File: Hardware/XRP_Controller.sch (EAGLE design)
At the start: 75 parts, among them J1 POWER_JACKPOWER_JACK_SLOT, J12 Vertical Qwiic Connector, J13 Vertical Qwiic Connector, J14 Vertical Qwiic Connector, J3 JST_6_PIN_VERTICAL, J4 JST_6_PIN_VERTICAL, J5 JST_6_PIN_VERTICAL, J6 JST_6_PIN_VERTICAL, J9 Vertical Qwiic Connector, Q3 20V/4.2A/52mΩ/1.4W, Q4 20V/4.2A/52mΩ/1.4W, Q5 20V/4.2A/52mΩ/1.4W, Q6 20V/4.2A/52mΩ/1.4W, U1 RPI_PICO_W, U2 AP63357, U4 LSM6DS0, U5 DRV8835, U6 DRV8835

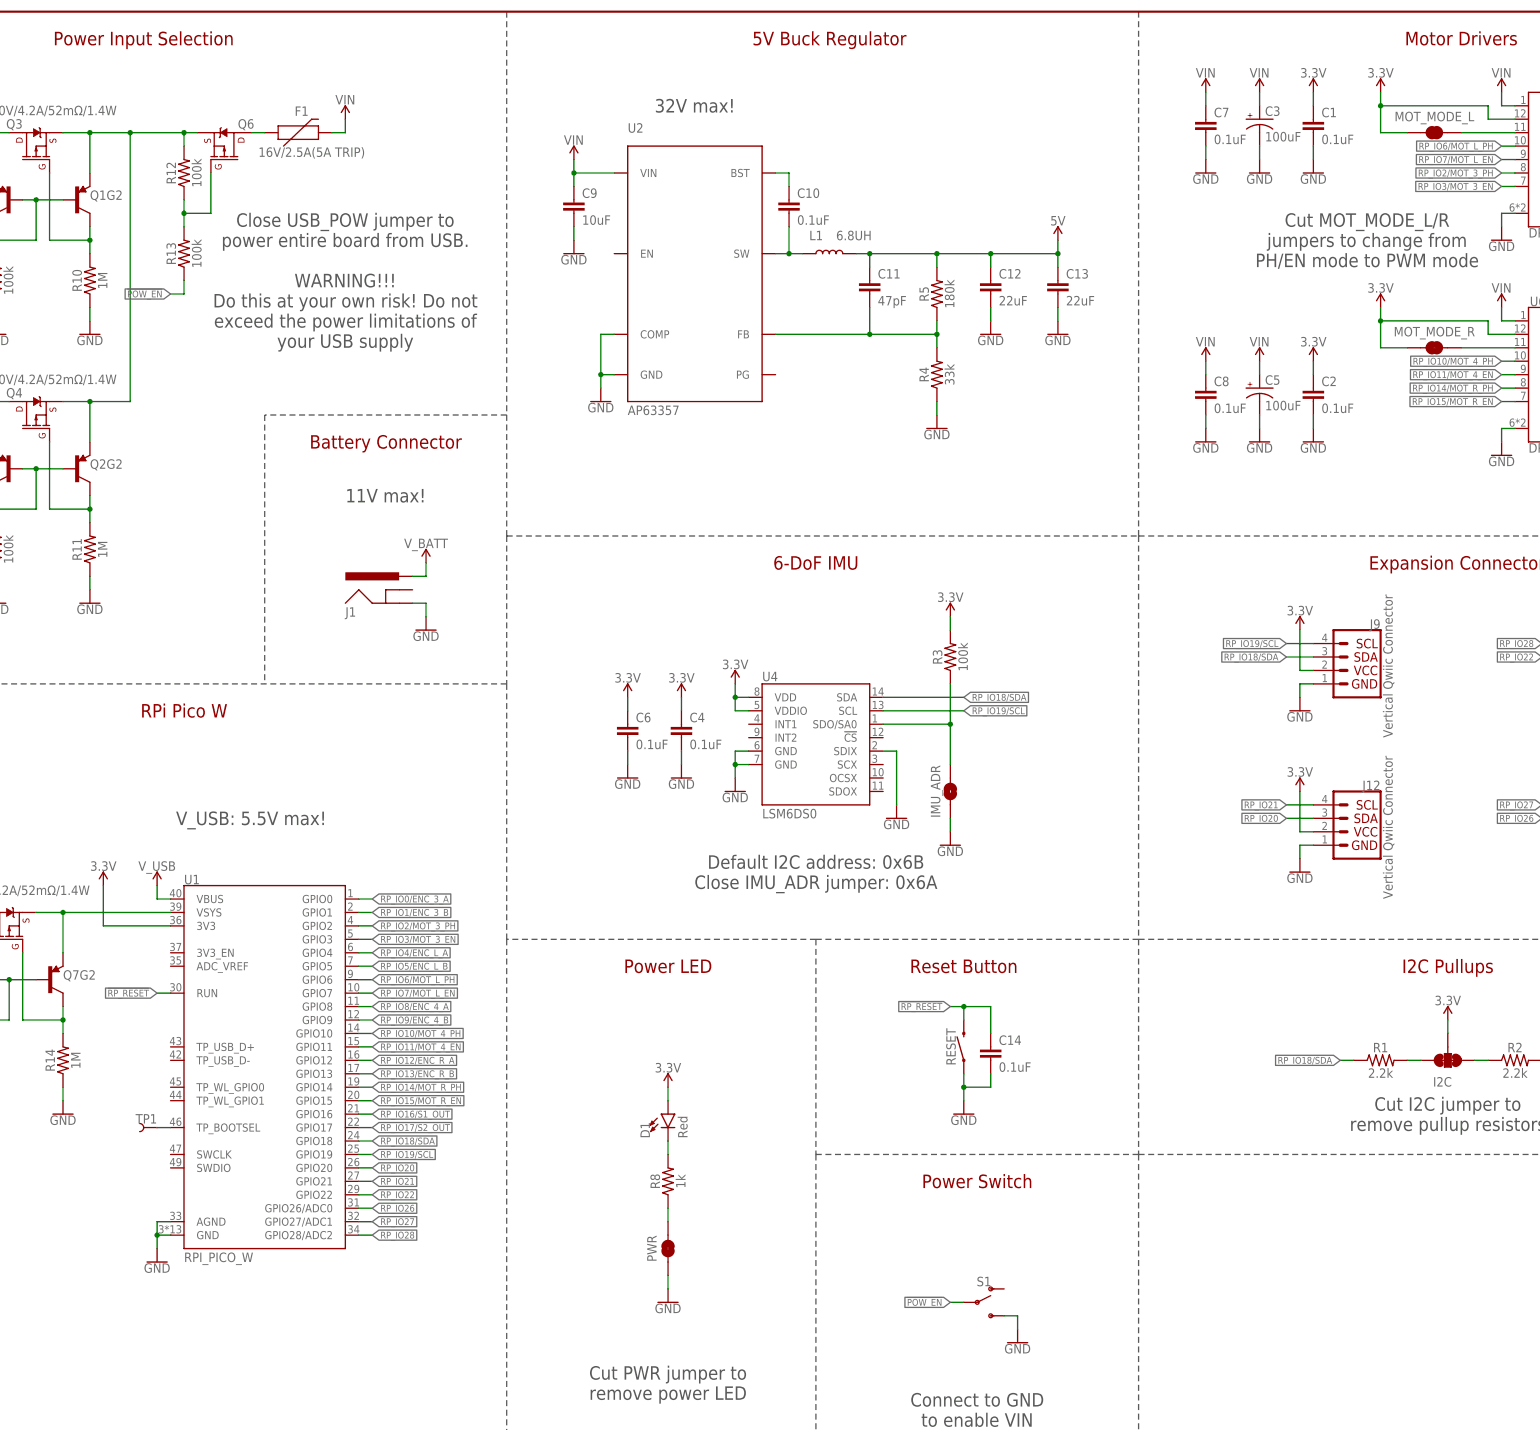
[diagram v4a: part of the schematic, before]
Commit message: Design review updates
Pico footprint:

Change pad and paste geometry based on DFM feedback (no copper or paste under the inner holes of the Pico's pads), and over paste outside of pads for better fillets)
Reduce paste under test points
Remove paste from USB PTH pads

Schematic:

Nudge power MOSFET to prevent !POW_EN! flag from overlapping net
Remove "32V max" from 5V buck to avoid confusion with 11V max for VIN

Board:

Improve GND continuity
Add test points for 5V buck EN and PG
Fix motor connector silk labels
Remove acid traps at encoder pins
Approve erroneous DRC errors
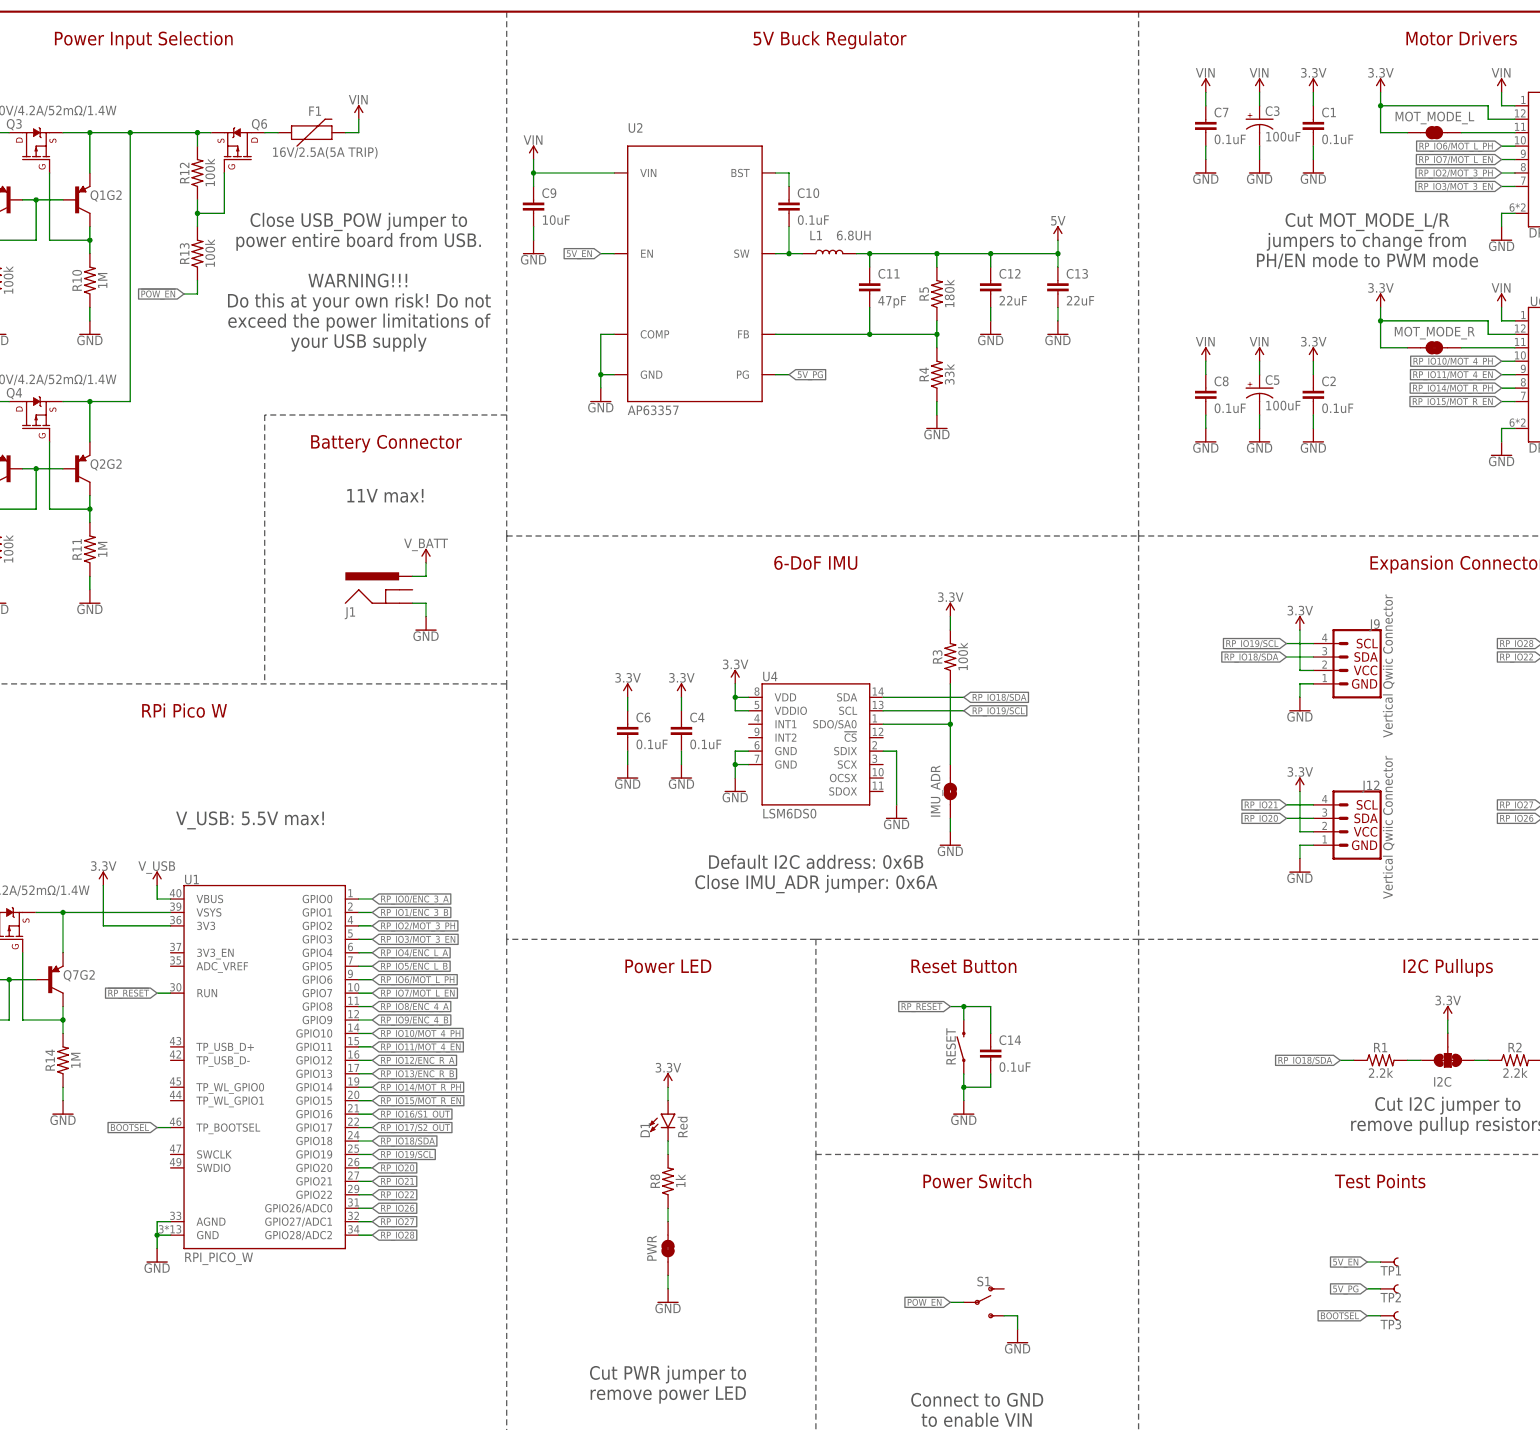
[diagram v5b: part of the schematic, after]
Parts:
- added TP2, TP3: TEST-POINT3X5, SparkFun-Connectors:TEST-POINT3X5
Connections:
- removed net N$18: TP1.1, U1.TP_BOOTSEL
- new net 5V_EN: TP1.1, U2.EN
- new net 5V_PG: TP2.1, U2.PG
- new net BOOTSEL: TP3.1, U1.TP_BOOTSEL
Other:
- note added: "Test Points"
- note removed: "32V max!"
- moved on the sheet: C9, F1, Q6, R12, R13, TP1

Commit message: v02 updates
Bump version number
Add tKeepout, tName and tValue to Pico W footprint
Reorganize schematic
Change servo header to locking footprint
Add test points for all GPIO pins
Add inverted Qwiic logo
Add selective solder paths to layer 48
Add barrel polarity silk to bottom
Add PTH silk labels to bottom
Add axes silk to bottom
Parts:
- removed LOGO2: QWIIC_LOGO_5MM, SparkFun-Aesthetics:QWIIC_LOGO_5MM
- added TP10, TP11, TP12, TP13, TP14, TP15, TP16, TP17, TP18, TP19, TP20, TP21, TP22, TP23, TP24, TP25, TP26, TP27, TP28, TP29, TP30, TP31, TP32, TP33, TP34, TP35, TP36, TP4, TP5, TP6, TP7, TP8, TP9: TEST-POINT3X5, SparkFun-Connectors:TEST-POINT3X5
- J7, J8: device SparkFun-Connectors:CONN_031X03_NO_SILK -> SparkFun-Connectors:CONN_03LOCK_NO_SILK
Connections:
- net N$12 renamed V_SYS
- net N$17 renamed V_POW
- net 3.3V: now also TP33.1
- net 5V_EN: now also TP34.1; no longer TP1.1
- net 5V_PG: now also TP35.1; no longer TP2.1
- net BOOTSEL: now also TP36.1; no longer TP3.1
- net GND: now also J8.3; no longer J8.1
- net MOT_3_N: now also TP26.1
- net MOT_3_P: now also TP25.1
- net MOT_4_N: now also TP31.1
- net MOT_4_P: now also TP29.1
- net MOT_L_N: now also TP28.1
- net MOT_L_P: now also TP27.1
- net MOT_R_N: now also TP32.1
- net MOT_R_P: now also TP30.1
- net RP_IO0/ENC_3_A: now also TP1.1
- net RP_IO1/ENC_3_B: now also TP2.1
- net RP_IO10/MOT_4_PH: now also TP11.1
- net RP_IO11/MOT_4_EN: now also TP12.1
- net RP_IO12/ENC_R_A: now also TP13.1
- net RP_IO13/ENC_R_B: now also TP14.1
- net RP_IO14/MOT_R_PH: now also TP15.1
- net RP_IO15/MOT_R_EN: now also TP16.1
- net RP_IO17/S2_OUT: now also J8.1; no longer J8.3
- net RP_IO18/SDA: now also TP17.1
- net RP_IO19/SCL: now also TP18.1
- net RP_IO2/MOT_3_PH: now also TP3.1
- net RP_IO20: now also TP19.1
- net RP_IO21: now also TP20.1
- net RP_IO22: now also TP21.1
- net RP_IO26: now also TP22.1
- net RP_IO27: now also TP23.1
- net RP_IO28: now also TP24.1
- net RP_IO3/MOT_3_EN: now also TP4.1
- net RP_IO4/ENC_L_A: now also TP5.1
- net RP_IO5/ENC_L_B: now also TP6.1
- net RP_IO6/MOT_L_PH: now also TP7.1
- net RP_IO7/MOT_L_EN: now also TP8.1
- net RP_IO8/ENC_4_A: now also TP9.1
- net RP_IO9/ENC_4_B: now also TP10.1
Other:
- note added: "Close USB_POW jumper to power entire board from USB. WARNING!!! Do this at your own risk! Do not exceed USB power limitations!"
- note added: "Power Selection Perfect Diode Circuits"
- note added: "V_SYS: 5.5V max!"
- note added: "v02"
- note removed: "Close USB_POW jumper to power entire board from USB. WARNING!!! Do this at your own risk! Do not exceed the power limitations of your USB supply"
- note removed: "Power Input Selection"
- note removed: "V_USB: 5.5V max!"
- note removed: "v01"
- moved on the sheet: C1, C10, C11, C12, C13, C14, C2, C3, C4, C5, C6, C7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
